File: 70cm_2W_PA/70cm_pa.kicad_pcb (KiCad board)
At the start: 2 copper layers, 48.3 x 48.3 mm, 22 parts, among them J1 Conn_Coaxial, J2 Conn_Coaxial, U1 M68710L, U2 LM75B

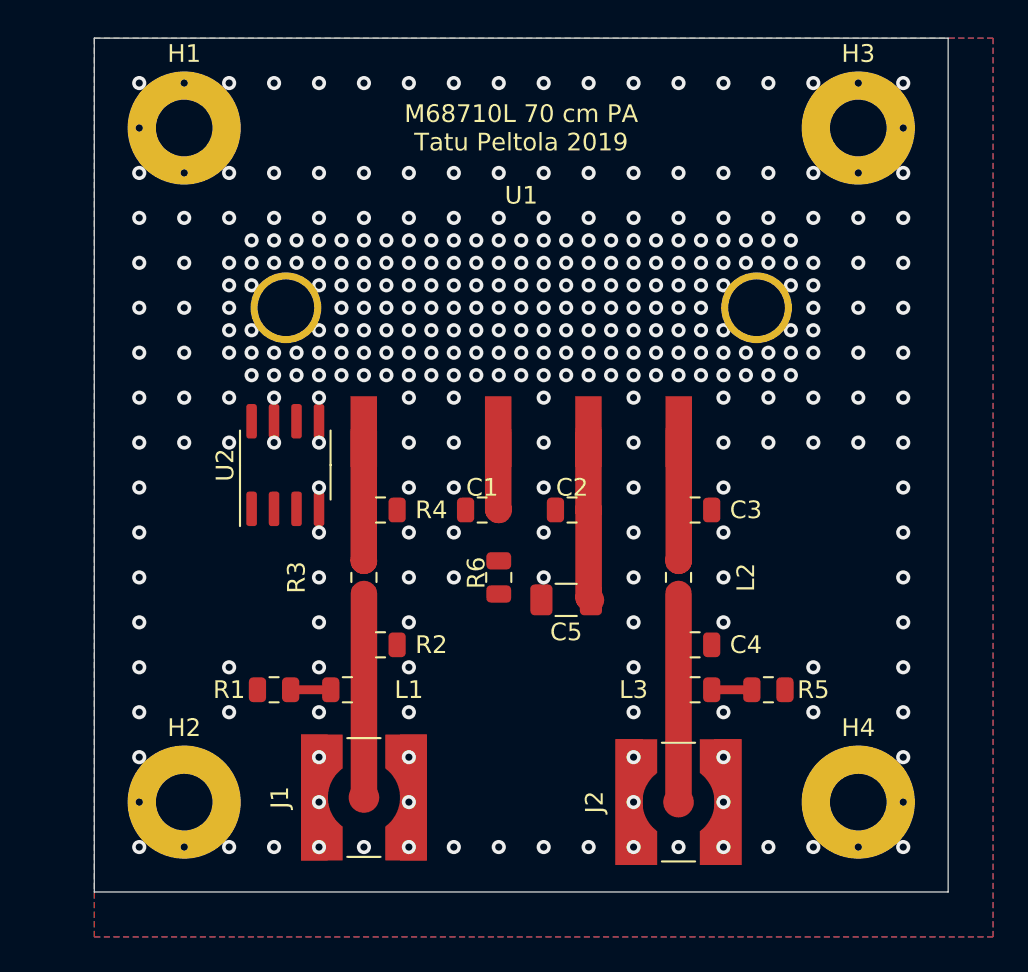
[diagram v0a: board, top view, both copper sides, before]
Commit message: Schematic fixes and a bit of layout
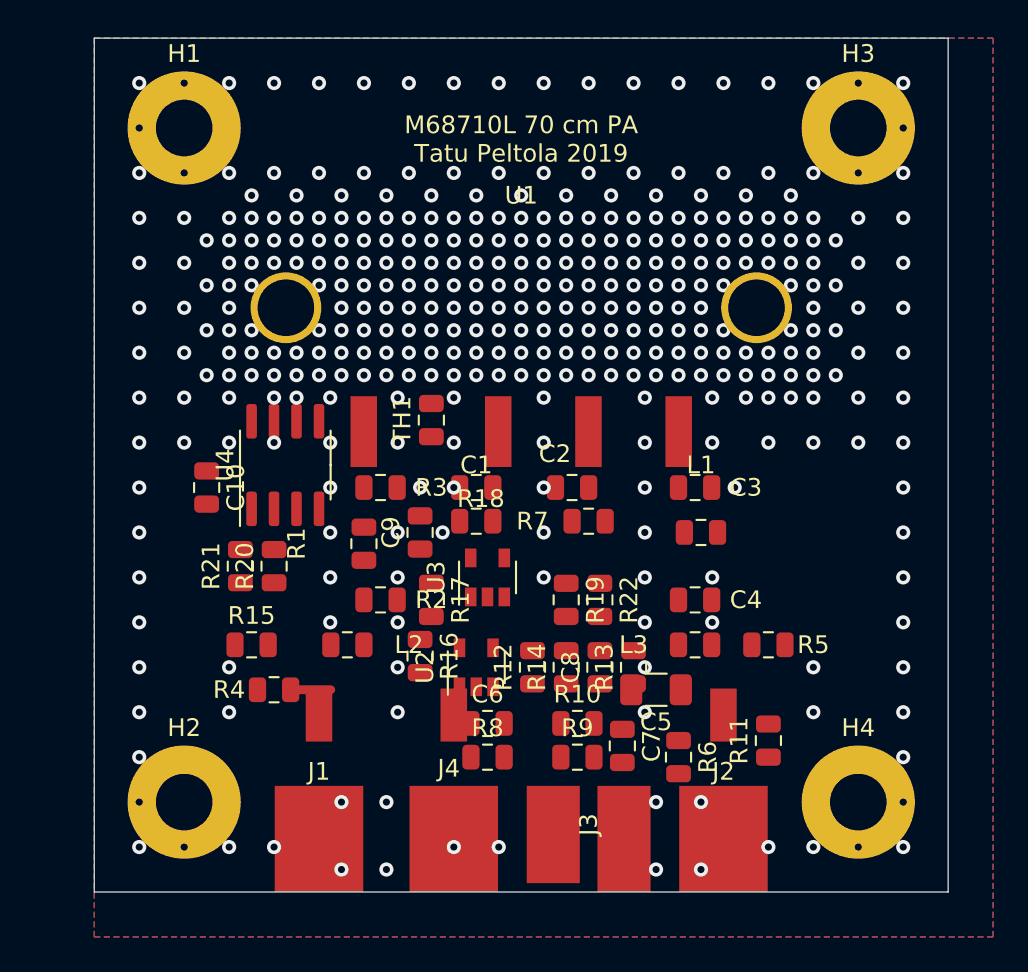
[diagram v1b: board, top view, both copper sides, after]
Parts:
- added C10: 100n, Capacitor_SMD:C_0805_2012Metric, F.Cu at (31.8, 50.8)
- added C6: 2u2, Capacitor_SMD:C_0805_2012Metric, F.Cu at (47.6, 64.1)
- added C7: 2u2, Capacitor_SMD:C_0805_2012Metric, F.Cu at (55.2, 65.4)
- added C8: 1n, Capacitor_SMD:C_0805_2012Metric, F.Cu at (54.0, 61.0)
- added C9: 100n, Capacitor_SMD:C_0805_2012Metric, F.Cu at (43.8, 53.3)
- added J3: Conn_01x02, 70cm_pa:DC_Pad, F.Cu at (53.3, 73.7)
- added J4: ~, 70cm_pa:Pigtail, F.Cu at (45.7, 73.7)
- added R10: ~, Resistor_SMD:R_0805_2012Metric, F.Cu at (52.7, 64.1)
- added R11: 1, Resistor_SMD:R_0805_2012Metric, F.Cu at (63.5, 65.1)
- added R12: ~, Resistor_SMD:R_0805_2012Metric, F.Cu at (50.2, 61.0)
- added R13: 68k, Resistor_SMD:R_0805_2012Metric, F.Cu at (55.9, 61.0)
- added R14: ~, Resistor_SMD:R_0805_2012Metric, F.Cu at (52.1, 61.0)
- added R15: 0, Resistor_SMD:R_0805_2012Metric, F.Cu at (34.3, 59.7)
- added R16: 100k, Resistor_SMD:R_0805_2012Metric, F.Cu at (43.8, 60.3)
- added R17: 100k, Resistor_SMD:R_0805_2012Metric, F.Cu at (44.5, 57.1)
- added R19: 1k, Resistor_SMD:R_0805_2012Metric, F.Cu at (52.1, 57.1)
- added R20: 1k, Resistor_SMD:R_0805_2012Metric, F.Cu at (35.6, 55.2)
- added R21: 1k, Resistor_SMD:R_0805_2012Metric, F.Cu at (33.7, 55.2)
- added R22: 100k, Resistor_SMD:R_0805_2012Metric, F.Cu at (54.0, 57.1)
- added R6: 0, Resistor_SMD:R_0805_2012Metric, F.Cu at (58.4, 66.0)
- added R7: 0, Resistor_SMD:R_0805_2012Metric, F.Cu at (53.3, 52.7)
- added R8: 0, Resistor_SMD:R_0805_2012Metric, F.Cu at (47.6, 66.0)
- added R9: 100k, Resistor_SMD:R_0805_2012Metric, F.Cu at (52.7, 66.0)
- added TH1: ~, Resistor_SMD:R_0805_2012Metric, F.Cu at (44.5, 47.0)
- added U2: MIC5205YM5, Package_TO_SOT_SMD:SOT-23-5, F.Cu at (47.0, 61.0)
- added U3: SN74LV1T08, Package_TO_SOT_SMD:SOT-23-5, F.Cu at (47.6, 55.9)
- J1, J2: value Conn_Coaxial -> ~; footprint Connector_Coaxial:SMA_Amphenol_132134-10_Vertical -> 70cm_pa:Pigtail
- moved C5 7.18 mm to (57.1, 62.2)
- moved J1 5.91 mm to (38.1, 73.7), turned to 0 degrees
- moved J2 5.68 mm to (61.0, 73.7), turned to 0 degrees
- moved R18 3.42 mm to (47.0, 52.7), turned to 180 degrees
- moved L1 2.84 mm to (59.7, 53.3), turned to 0 degrees
- moved C4 2.54 mm to (59.4, 57.1)
- moved L2 2.54 mm to (39.7, 59.7)
- moved L3 2.54 mm to (59.4, 59.7)
- moved R2 2.54 mm to (41.6, 57.1)
- moved R5 2.54 mm to (63.5, 59.7)
- moved R1 1.91 mm to (40.6, 54.0)
- moved C1 1.31 mm to (47.0, 50.8)
- moved C2 1.27 mm to (52.4, 50.8)
- moved C3 1.27 mm to (59.4, 50.8)
- moved R3 1.27 mm to (41.6, 50.8)
- renumbered L2 to L1, L1 to L2, R3 to R1, R6 to R18, R4 to R3, R1 to R4, U2 to U4
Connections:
- net /PA_PO renamed /PA_out
- net /PA_Pin renamed /PA_in
- net Net-(C4-Pad1) renamed /RF_out
- net Net-(J1-Pad1) renamed /RF_in
- C5 pad 1: /PA_VDD -> /V_supply
- R18 pad 2: /BIAS -> Net-(R18-Pad2)
- U4 pad 8: /LogicVDD -> /LM_VDD
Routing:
- net /RF_out: track 11.8 -> 0.00 mm
- net /RF_in: track 11.5 -> 0.00 mm
- net /PA_VDD: track 9.57 -> 0.00 mm
- net /PA_out: track 7.31 -> 0.00 mm
- net /PA_in: track 7.31 -> 0.00 mm
- net /PA_VGG: track 4.44 -> 0.00 mm
- net Net-(L3-Pad2): track 2.27 -> 0.00 mm
- net GND: vias 340 -> 368
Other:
- net class Default: trace_width 1.5 -> 1.4

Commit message: Most components connected in layout (M68710L)
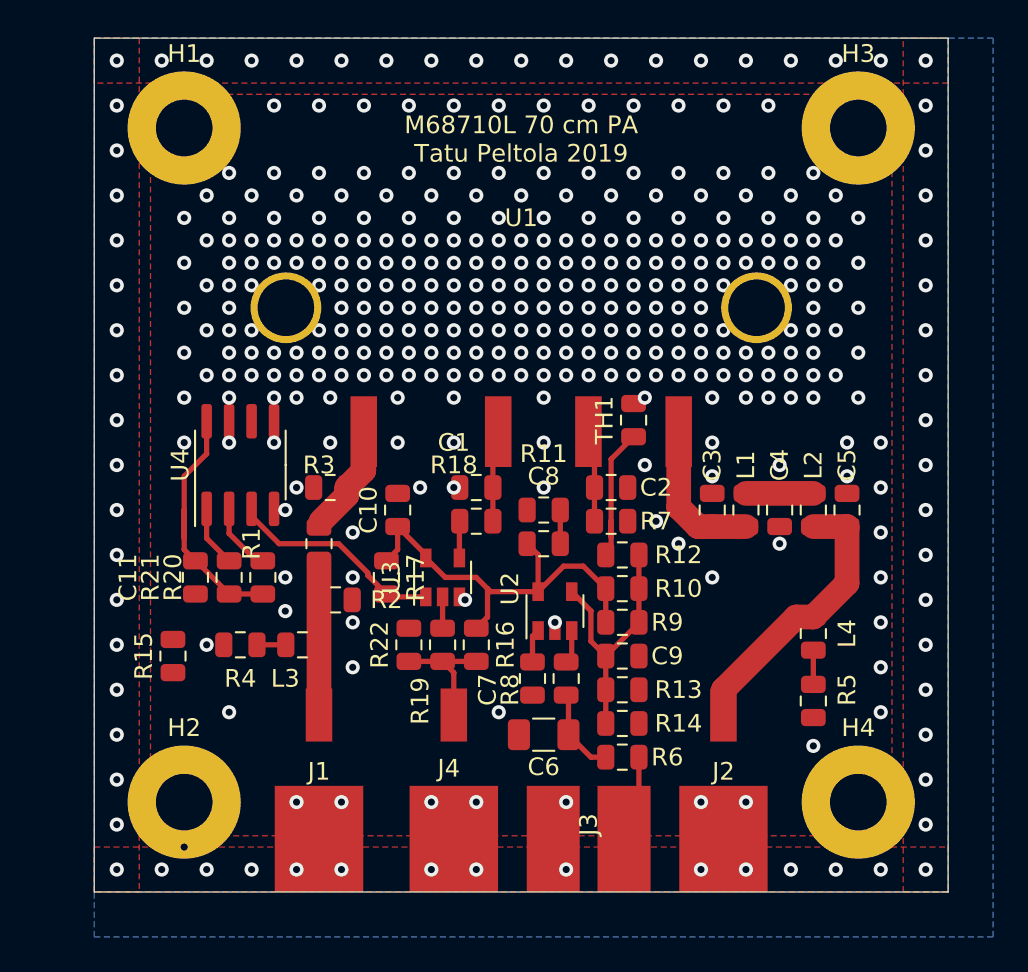
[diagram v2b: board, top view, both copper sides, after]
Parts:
- removed the C9 at (43.8, 53.3)
- added C10: 100n, Capacitor_SMD:C_0805_2012Metric, F.Cu at (42.5, 52.1)
- added C5: TBD, Capacitor_SMD:C_0805_2012Metric, F.Cu at (67.9, 52.1)
- added L2: TBD, Inductor_SMD:L_0805_2012Metric, F.Cu at (66.0, 52.1)
- moved R11 18.2 mm to (50.8, 52.1), turned to 180 degrees
- moved C8 12.3 mm to (50.8, 54.0), turned to 0 degrees
- moved TH1 11.4 mm to (55.9, 47.0)
- moved R22 11.1 mm to (43.2, 59.7), turned to 90 degrees
- moved R12 8.13 mm to (55.2, 54.6), turned to 0 degrees
- moved R10 8.03 mm to (55.2, 56.5)
- moved R9 8.03 mm to (55.2, 58.4)
- moved R19 7.43 mm to (45.1, 59.7)
- moved C4 6.97 mm to (64.1, 52.1), turned to 270 degrees
- moved C6 6.84 mm to (50.8, 64.8)
- moved L4 6.71 mm to (66.0, 59.1), turned to 270 degrees
- moved R8 6.29 mm to (52.1, 61.6), turned to 270 degrees
- moved U2 5.46 mm to (51.4, 57.8)
- moved C11 5.12 mm to (31.1, 55.9)
- moved R14 4.49 mm to (55.2, 64.1), turned to 0 degrees
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- renumbered C10 to C11, C5 to C6, C6 to C7, C7 to C8, C8 to C9, L2 to L3, L3 to L4
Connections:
- net Net-(C8-Pad1) renamed /REG_ADJ
- C4 pad 1: /RF_out -> Net-(C4-Pad1)
- L1 pad 2: /RF_out -> Net-(C4-Pad1)
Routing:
- net VCC: track 0.00 -> 24.4 mm, vias 0 -> 1
- net /RF_out: track 0.00 -> 16.0 mm
- net /LM_VDD: track 0.00 -> 14.9 mm
- net /REG_ADJ: track 0.00 -> 14.7 mm
- net /OS: track 0.00 -> 12.2 mm
- net /PA_out: track 0.00 -> 8.53 mm
- net /RF_in: track 0.00 -> 8.41 mm
- net /NTC: track 0.00 -> 7.77 mm
- net /EN: track 0.00 -> 7.11 mm
- net /PA_in: track 0.00 -> 6.07 mm
- net /PA_VDD: track 0.00 -> 5.21 mm
- net /PA_VGG: track 0.00 -> 5.19 mm
- net /V_in: track 0.00 -> 4.97 mm
- net /V_supply: track 0.00 -> 4.92 mm
- net /SCL: track 0.00 -> 3.94 mm
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
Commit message: M68710L: rearrange layout a bit
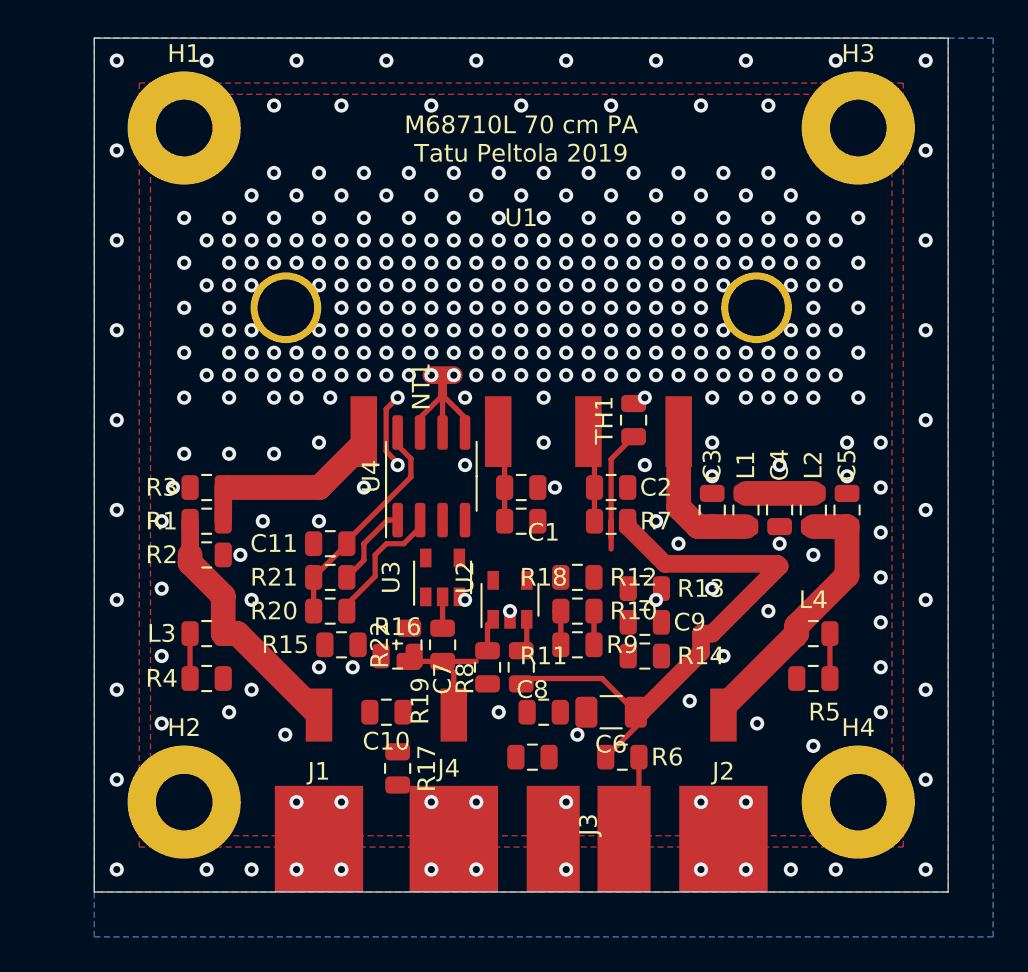
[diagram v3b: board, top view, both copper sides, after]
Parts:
- added NT1: ~, NetTie:NetTie-2_SMD_Pad0.5mm, F.Cu at (45.1, 45.1)
- R8: value 0 -> 1
- moved C8 12.1 mm to (50.2, 66.0)
- moved C10 11.4 mm to (41.9, 63.5), turned to 180 degrees
- moved R11 11.4 mm to (50.8, 63.5)
- moved U4 10.8 mm to (44.5, 50.2)
- moved R17 10.8 mm to (42.5, 66.7)
- moved R15 9.55 mm to (39.4, 59.7), turned to 0 degrees
- moved C11 7.85 mm to (38.7, 54.0), turned to 180 degrees
- moved R2 7.72 mm to (31.8, 54.6)
- moved R3 6.98 mm to (31.8, 50.8)
- moved R1 6.48 mm to (31.8, 52.7), turned to 180 degrees
- moved R13 5.85 mm to (56.5, 56.5)
- moved R21 5.71 mm to (38.7, 55.9), turned to 0 degrees
- moved L3 5.45 mm to (31.8, 59.1)
- moved R16 4.49 mm to (42.5, 60.3), turned to 0 degrees
- moved R20 4.26 mm to (38.7, 57.8), turned to 0 degrees
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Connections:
- U4 pad 5: GND -> Net-(NT1-Pad1)
- U4 pad 6: GND -> Net-(NT1-Pad1)
- U4 pad 7: GND -> Net-(NT1-Pad1)
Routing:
- net /V_supply: track 4.92 -> 32.8 mm
- net VCC: track 24.4 -> 2.24 mm, vias 1 -> 0
- net /REG_ADJ: track 14.7 -> 1.91 mm
- net /OS: track 12.2 -> 0.00 mm
- net Net-(NT1-Pad1): track 0.00 -> 7.37 mm
- net /RF_in: track 8.41 -> 14.4 mm
- net GND: track 0.00 -> 5.62 mm, vias 375 -> 347
- net /PA_in: track 6.07 -> 11.2 mm
- net /SCL: track 3.94 -> 7.44 mm
- net /LM_VDD: track 14.9 -> 12.7 mm
- net Net-(R18-Pad2): track 2.08 -> 0.00 mm
- net Net-(C8-Pad2): track 1.91 -> 0.00 mm
- net /SDA: track 3.46 -> 5.13 mm
- net Net-(L3-Pad2): track 1.63 -> 2.54 mm
- net Net-(L4-Pad2): track 1.94 -> 2.54 mm
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
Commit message: M68710L: more layout
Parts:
- added C7: 2u2, Capacitor_SMD:C_0805_2012Metric, F.Cu at (52.7, 65.4)
- C6: value 10u -> 100u; footprint Capacitor_SMD:C_1206_3216Metric -> Capacitor_Tantalum_SMD:CP_EIA-6032-15_Kemet-U
- moved R11 27.4 mm to (24.1, 57.1), turned to 90 degrees
- moved C9 27.3 mm to (23.5, 60.3)
- moved C11 17.8 mm to (24.1, 62.9)
- moved R17 11.7 mm to (45.1, 55.2), turned to 0 degrees
- moved R13 5.12 mm to (55.9, 61.6), turned to 270 degrees
- moved R14 4.62 mm to (52.1, 61.6), turned to 270 degrees
- moved U3 4.37 mm to (49.0, 54.0)
- moved C10 4.07 mm to (54.0, 61.6), turned to 270 degrees
- moved R12 3.70 mm to (55.9, 57.8), turned to 270 degrees
- moved C6 2.69 mm to (52.7, 65.4)
- moved R6 2.62 mm to (57.8, 65.4), turned to 270 degrees
- moved R18 2.50 mm to (51.9, 52.1), turned to 270 degrees
- moved R22 2.01 mm to (45.1, 60.3), turned to 0 degrees
- moved R9 2.01 mm to (52.1, 57.8), turned to 270 degrees
- moved R19 1.91 mm to (45.1, 57.8), turned to 180 degrees
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- renumbered C9 to C10, C10 to C11, C11 to C12, C7 to C8, C8 to C9
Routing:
- net /V_supply: track 32.8 -> 16.2 mm
- net GND: track 5.62 -> 17.2 mm, vias 347 -> 359
- net VCC: track 2.24 -> 13.2 mm
- net /REG_ADJ: track 1.91 -> 11.6 mm
- net Net-(C8-Pad1): track 3.81 -> 7.28 mm
- net /NTC: track 7.77 -> 10.9 mm
- net Net-(R19-Pad1): track 1.77 -> 4.82 mm
- net /OS: track 0.00 -> 2.99 mm
- net /PA_VGG: track 5.22 -> 8.11 mm
- net Net-(R18-Pad2): track 0.00 -> 2.03 mm
- net /EN: track 7.11 -> 6.54 mm

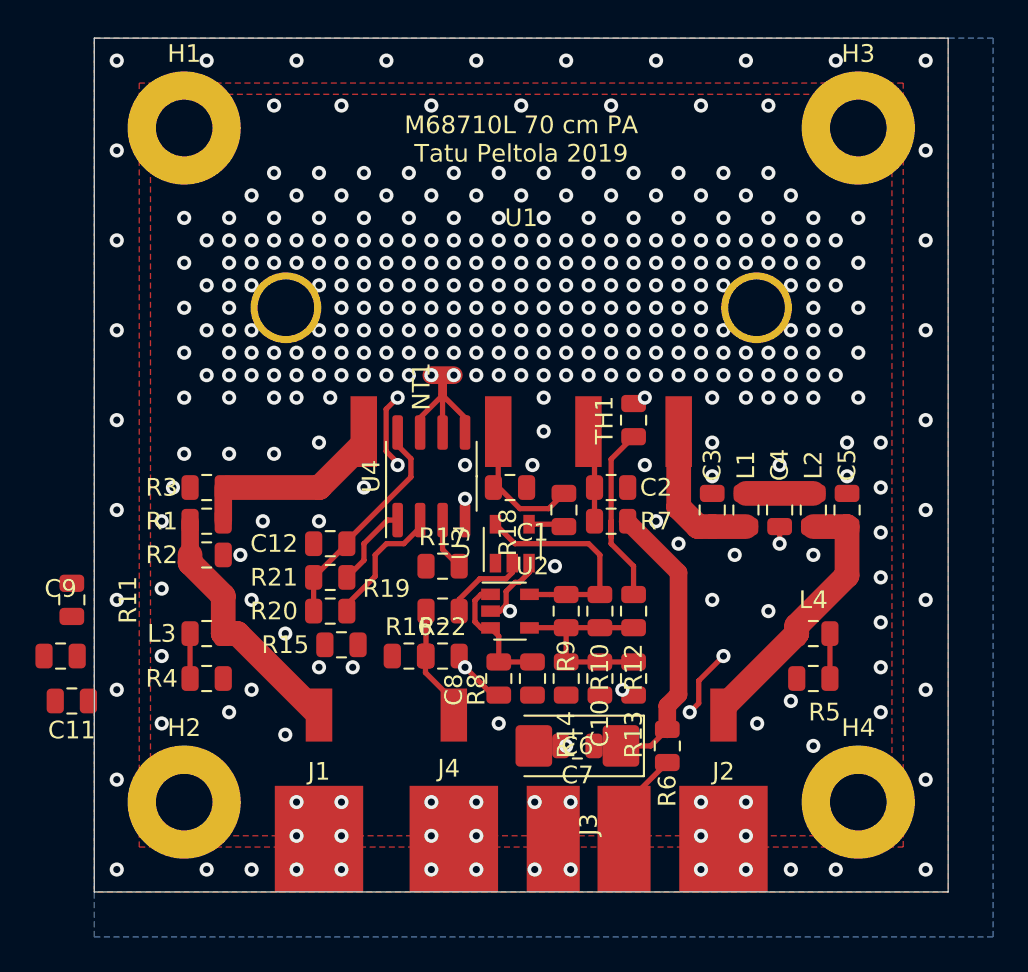
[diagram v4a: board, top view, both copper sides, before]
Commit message: M68710L: remove LM75
LM75 operated from the gate bias supply which could become a problem
if bias below 2.8 V is desired. Different supplies might also become
a problem if the I2C were connected to external logic.

LM75 also took more PCB area.
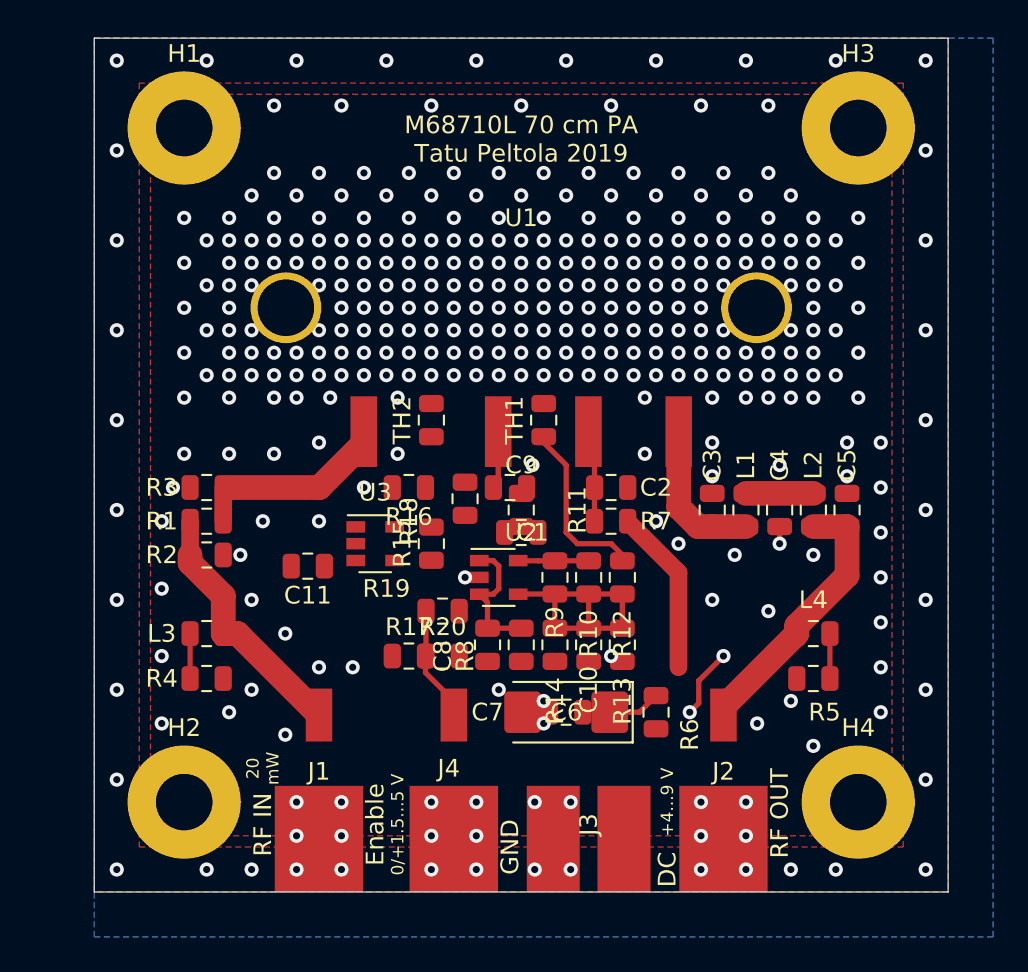
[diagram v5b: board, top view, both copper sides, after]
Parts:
- removed C12: 100n, Capacitor_SMD:C_0805_2012Metric
- removed NT1: ~, NetTie:NetTie-2_SMD_Pad0.5mm
- removed the R20 at (38.7, 57.8)
- removed R21: 1k, Resistor_SMD:R_0805_2012Metric
- removed U4: LM75B, Package_SO:SOIC-8_3.9x4.9mm_P1.27mm
- added TH2: 100k, Resistor_SMD:R_0805_2012Metric, F.Cu at (44.5, 47.0)
- R15: value 0 -> ~
- R16: renamed from R17; value 100k -> 33k
- moved C9 27.0 mm to (49.5, 53.3)
- moved R11 25.9 mm to (49.5, 52.1)
- moved C11 15.4 mm to (37.5, 55.2)
- moved U3 7.75 mm to (41.3, 54.0), turned to 0 degrees
- moved R15 7.65 mm to (44.5, 54.0), turned to 90 degrees
- moved R18 5.62 mm to (46.4, 51.4)
- moved TH1 5.08 mm to (50.8, 47.0)
- moved R16 4.84 mm to (43.2, 50.8), turned to 180 degrees
- moved R13 2.01 mm to (55.2, 59.7)
- moved C10 2.01 mm to (53.3, 59.7)
- moved C6 2.01 mm to (52.1, 63.5)
- moved C7 2.01 mm to (52.1, 63.5)
- moved C8 2.01 mm to (47.6, 59.7)
- moved R14 2.01 mm to (51.4, 59.7)
- moved R6 2.01 mm to (57.1, 63.5)
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- renumbered R16 to R17, R22 to R20
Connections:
- net /NTC renamed /NTC1
- R15 pad 1: /LM_VDD -> Net-(R15-Pad1)
- R15 pad 2: VCC -> /NTC2
- R16 pad 2: /OS -> /NTC2
- R18 pad 2: Net-(R18-Pad2) -> Net-(R15-Pad1)
- U3 pad 1: /OS -> /NTC2
- U3 pad 4: Net-(R18-Pad2) -> Net-(R15-Pad1)
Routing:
- net /LM_VDD: track 12.7 -> 0.00 mm
- net GND: track 17.2 -> 4.93 mm, vias 359 -> 354
- net VCC: track 13.2 -> 4.32 mm
- net /SCL: track 7.44 -> 0.00 mm
- net Net-(NT1-Pad1): track 7.37 -> 0.00 mm
- net /SDA: track 5.13 -> 0.00 mm
- net /PA_VGG: track 8.11 -> 3.27 mm
- net Net-(R19-Pad1): track 4.82 -> 0.00 mm
- net /REG_ADJ: track 11.6 -> 15.5 mm
- net /V_supply: track 16.2 -> 13.0 mm
- net /OS: track 2.99 -> 0.00 mm
- net /V_in: track 5.33 -> 2.51 mm
- net Net-(R18-Pad2): track 2.03 -> 0.00 mm
- net /NTC1: track 10.9 -> 9.97 mm
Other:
- board text added: "+4...9 V"
- board text added: "0/+1.5...5 V"
- board text added: "20 mW"
- board text added: "DC"
- board text added: "Enable"
- board text added: "GND"
- board text added: "RF IN"
- board text added: "RF OUT"
